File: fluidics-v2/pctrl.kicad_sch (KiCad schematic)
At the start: 8 parts, among them U15 ADS1115IDGS, U16 AD5624RBRMZ-3

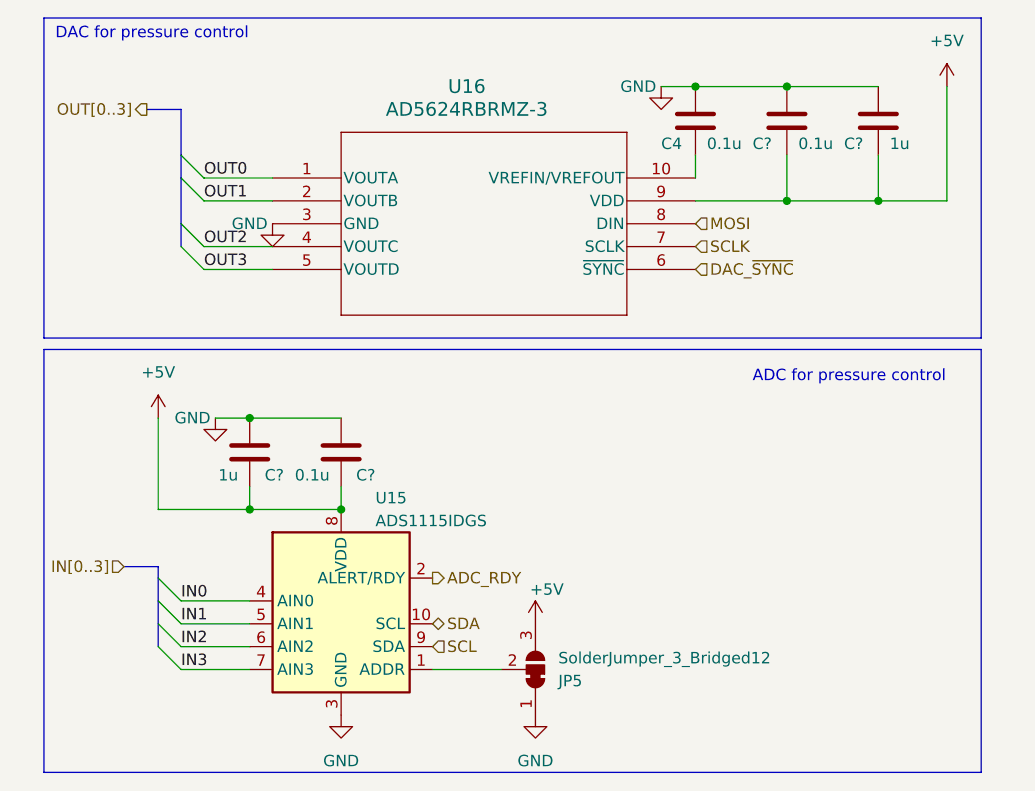
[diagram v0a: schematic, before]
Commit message: added new connector for motor control daughter board. began layout
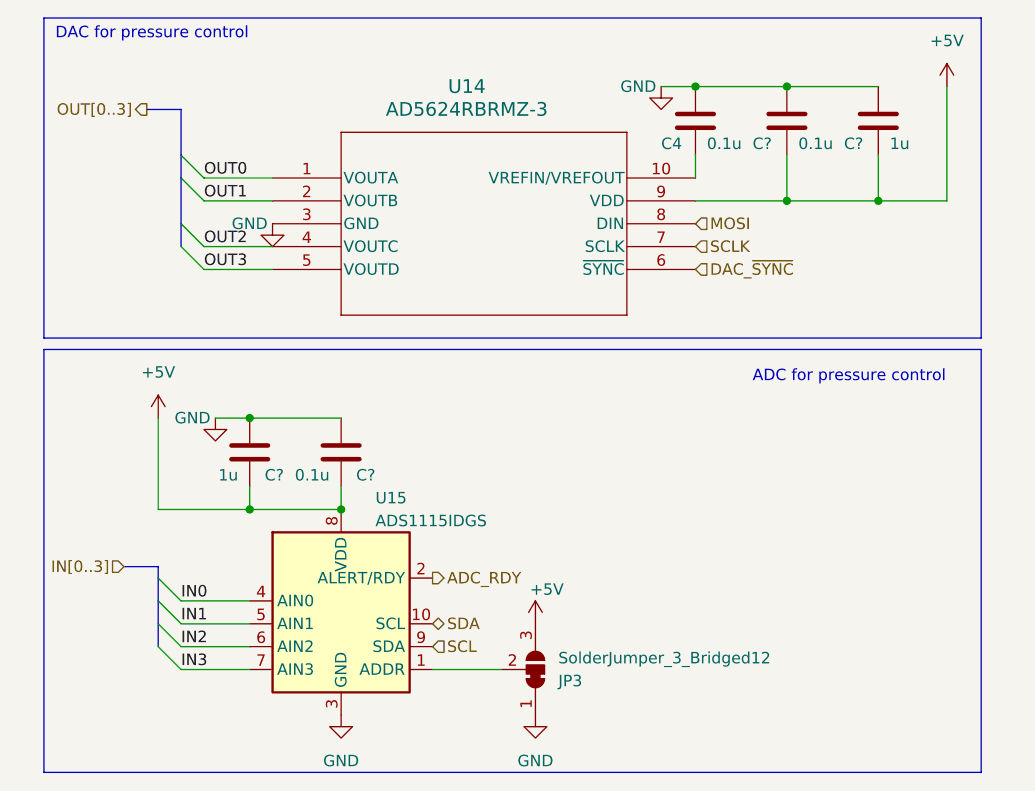
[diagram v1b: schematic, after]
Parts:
- JP3: renamed from JP5; footprint (none) -> Jumper:SolderJumper-3_P1.3mm_Bridged12_Pad1.0x1.5mm_NumberLabels
- U14: renamed from U16; footprint RM_10_ADI -> Package_SO:MSOP-10_3x3mm_P0.5mm
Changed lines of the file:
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@@
   (symbol (lib_id "power:GND") (at 224.79 63.5 0) (unit 1)
     (in_bom yes) (on_board yes) (dnp no)
-    (property "Reference" "#PWR0175" (at 224.79 69.85 0)
+    (property "Reference" "#PWR0159" (at 224.79 69.85 0)
       (effects (font (size 1.27 1.27)) hide)
     )
@@
       (project "fluidics-v2"
         (path "/0ec91c42-8aad-437d-8c85-5e10f0e51fe0/41df25db-e2cd-4148-9d69-e83cb6b162f0"
-          (reference "#PWR0175") (unit 1)
+          (reference "#PWR0159") (unit 1)
         )
       )
@@
   (symbol (lib_id "power:GND") (at 189.23 133.35 0) (unit 1)
     (in_bom yes) (on_board yes) (dnp no) (fields_autoplaced)
-    (property "Reference" "#PWR0181" (at 189.23 139.7 0)
+    (property "Reference" "#PWR0156" (at 189.23 139.7 0)
       (effects (font (size 1.27 1.27)) hide)
     )
@@
       (project "fluidics-v2"
         (path "/0ec91c42-8aad-437d-8c85-5e10f0e51fe0/41df25db-e2cd-4148-9d69-e83cb6b162f0"
-          (reference "#PWR0181") (unit 1)
+          (reference "#PWR0156") (unit 1)
         )
       )
@@
         )
         (path "/0ec91c42-8aad-437d-8c85-5e10f0e51fe0/41df25db-e2cd-4148-9d69-e83cb6b162f0"
-          (reference "C39") (unit 1)
+          (reference "C25") (unit 1)
         )
       )
@@
         )
         (path "/0ec91c42-8aad-437d-8c85-5e10f0e51fe0/41df25db-e2cd-4148-9d69-e83cb6b162f0"
-          (reference "C36") (unit 1)
+          (reference "C28") (unit 1)
         )
       )
@@
   (symbol (lib_id "power:+5V") (at 210.82 123.19 0) (unit 1)
     (in_bom yes) (on_board yes) (dnp no)
-    (property "Reference" "#PWR0179" (at 210.82 127 0)
+    (property "Reference" "#PWR0157" (at 210.82 127 0)
       (effects (font (size 1.27 1.27)) hide)
     )
@@
       (project "fluidics-v2"
         (path "/0ec91c42-8aad-437d-8c85-5e10f0e51fe0/41df25db-e2cd-4148-9d69-e83cb6b162f0"
-          (reference "#PWR0179") (unit 1)
+          (reference "#PWR0157") (unit 1)
         )
       )
@@
   (symbol (lib_id "AD5624:AD5624RBRMZ-3") (at 160.02 73.66 0) (unit 1)
     (in_bom yes) (on_board yes) (dnp no) (fields_autoplaced)
-    (property "Reference" "U16" (at 203.2 63.5 0)
+    (property "Reference" "U14" (at 203.2 63.5 0)
       (effects (font (size 1.524 1.524)))
     )
@@
       (effects (font (size 1.524 1.524)))
     )
-    (property "Footprint" "RM_10_ADI" (at 160.02 73.66 0)
+    (property "Footprint" "Package_SO:MSOP-10_3x3mm_P0.5mm" (at 160.02 73.66 0)
       (effects (font (size 1.27 1.27) italic) hide)
     )
@@
       (project "fluidics-v2"
         (path "/0ec91c42-8aad-437d-8c85-5e10f0e51fe0/41df25db-e2cd-4148-9d69-e83cb6b162f0"
-          (reference "U16") (unit 1)
+          (reference "U14") (unit 1)
         )
       )
@@
         )
         (path "/0ec91c42-8aad-437d-8c85-5e10f0e51fe0/41df25db-e2cd-4148-9d69-e83cb6b162f0"
-          (reference "C38") (unit 1)
+          (reference "C26") (unit 1)
         )
       )
@@
   (symbol (lib_id "power:GND") (at 210.82 133.35 0) (unit 1)
     (in_bom yes) (on_board yes) (dnp no) (fields_autoplaced)
-    (property "Reference" "#PWR0180" (at 210.82 139.7 0)
+    (property "Reference" "#PWR0158" (at 210.82 139.7 0)
       (effects (font (size 1.27 1.27)) hide)
     )
@@
       (project "fluidics-v2"
         (path "/0ec91c42-8aad-437d-8c85-5e10f0e51fe0/41df25db-e2cd-4148-9d69-e83cb6b162f0"
-          (reference "#PWR0180") (unit 1)
+          (reference "#PWR0158") (unit 1)
         )
       )
@@
   (symbol (lib_id "power:GND") (at 181.61 78.74 0) (unit 1)
     (in_bom yes) (on_board yes) (dnp no)
-    (property "Reference" "#PWR0174" (at 181.61 85.09 0)
+    (property "Reference" "#PWR0155" (at 181.61 85.09 0)
       (effects (font (size 1.27 1.27)) hide)
     )
@@
       (project "fluidics-v2"
         (path "/0ec91c42-8aad-437d-8c85-5e10f0e51fe0/41df25db-e2cd-4148-9d69-e83cb6b162f0"
-          (reference "#PWR0174") (unit 1)
+          (reference "#PWR0155") (unit 1)
         )
       )
@@
   (symbol (lib_id "power:+5V") (at 256.54 63.5 0) (unit 1)
     (in_bom yes) (on_board yes) (dnp no) (fields_autoplaced)
-    (property "Reference" "#PWR0176" (at 256.54 67.31 0)
+    (property "Reference" "#PWR0160" (at 256.54 67.31 0)
       (effects (font (size 1.27 1.27)) hide)
     )
@@
       (project "fluidics-v2"
         (path "/0ec91c42-8aad-437d-8c85-5e10f0e51fe0/41df25db-e2cd-4148-9d69-e83cb6b162f0"
-          (reference "#PWR0176") (unit 1)
+          (reference "#PWR0160") (unit 1)
         )
       )
@@
         )
         (path "/0ec91c42-8aad-437d-8c85-5e10f0e51fe0/41df25db-e2cd-4148-9d69-e83cb6b162f0"
-          (reference "C35") (unit 1)
+          (reference "C27") (unit 1)
         )
       )
@@
   (symbol (lib_id "power:+5V") (at 168.91 100.33 0) (mirror y) (unit 1)
     (in_bom yes) (on_board yes) (dnp no) (fields_autoplaced)
-    (property "Reference" "#PWR0177" (at 168.91 104.14 0)
+    (property "Reference" "#PWR0153" (at 168.91 104.14 0)
       (effects (font (size 1.27 1.27)) hide)
     )
@@
       (project "fluidics-v2"
         (path "/0ec91c42-8aad-437d-8c85-5e10f0e51fe0/41df25db-e2cd-4148-9d69-e83cb6b162f0"
-          (reference "#PWR0177") (unit 1)
+          (reference "#PWR0153") (unit 1)
         )
       )
@@
   (symbol (lib_id "power:GND") (at 175.26 100.33 0) (unit 1)
     (in_bom yes) (on_board yes) (dnp no)
-    (property "Reference" "#PWR0178" (at 175.26 106.68 0)
+    (property "Reference" "#PWR0154" (at 175.26 106.68 0)
       (effects (font (size 1.27 1.27)) hide)
     )
@@
       (project "fluidics-v2"
         (path "/0ec91c42-8aad-437d-8c85-5e10f0e51fe0/41df25db-e2cd-4148-9d69-e83cb6b162f0"
-          (reference "#PWR0178") (unit 1)
+          (reference "#PWR0154") (unit 1)
         )
       )
@@
         )
         (path "/0ec91c42-8aad-437d-8c85-5e10f0e51fe0/41df25db-e2cd-4148-9d69-e83cb6b162f0"
-          (reference "C37") (unit 1)
+          (reference "C29") (unit 1)
         )
       )
@@
   (symbol (lib_id "Jumper:SolderJumper_3_Bridged12") (at 210.82 128.27 270) (mirror x) (unit 1)
     (in_bom yes) (on_board yes) (dnp no)
-    (property "Reference" "JP5" (at 213.36 129.54 90)
+    (property "Reference" "JP3" (at 213.36 129.54 90)
       (effects (font (size 1.27 1.27)) (justify left))
     )
@@
       (effects (font (size 1.27 1.27)) (justify left))
     )
-    (property "Footprint" "" (at 210.82 128.27 0)
+    (property "Footprint" "Jumper:SolderJumper-3_P1.3mm_Bridged12_Pad1.0x1.5mm_NumberLabels" (at 210.82 128.27 0)
       (effects (font (size 1.27 1.27)) hide)
     )
@@
       (project "fluidics-v2"
         (path "/0ec91c42-8aad-437d-8c85-5e10f0e51fe0/41df25db-e2cd-4148-9d69-e83cb6b162f0"
-          (reference "JP5") (unit 1)
-        )
-      )
+          (reference "JP3") (unit 1)
+        )
+      )
